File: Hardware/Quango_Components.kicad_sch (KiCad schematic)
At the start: 112 parts, among them J1 Conn_01x12_Male, J2 Conn_01x12_Male, J3 Conn_01x12_Male, J4 Conn_01x12_Male, J5 SWD_Header, J6 Eurorack_10_pin_power, Q1 MMBT3904, U1 LM1117-3.3, U2 STM32G473V, U3 LM1117-5.0, U4 PS508, U5 MCP6002, U6 AS3364, U7 AS3364, U8 AD5676, U9 MCP48CMB21, Y1 8MHz 20pF

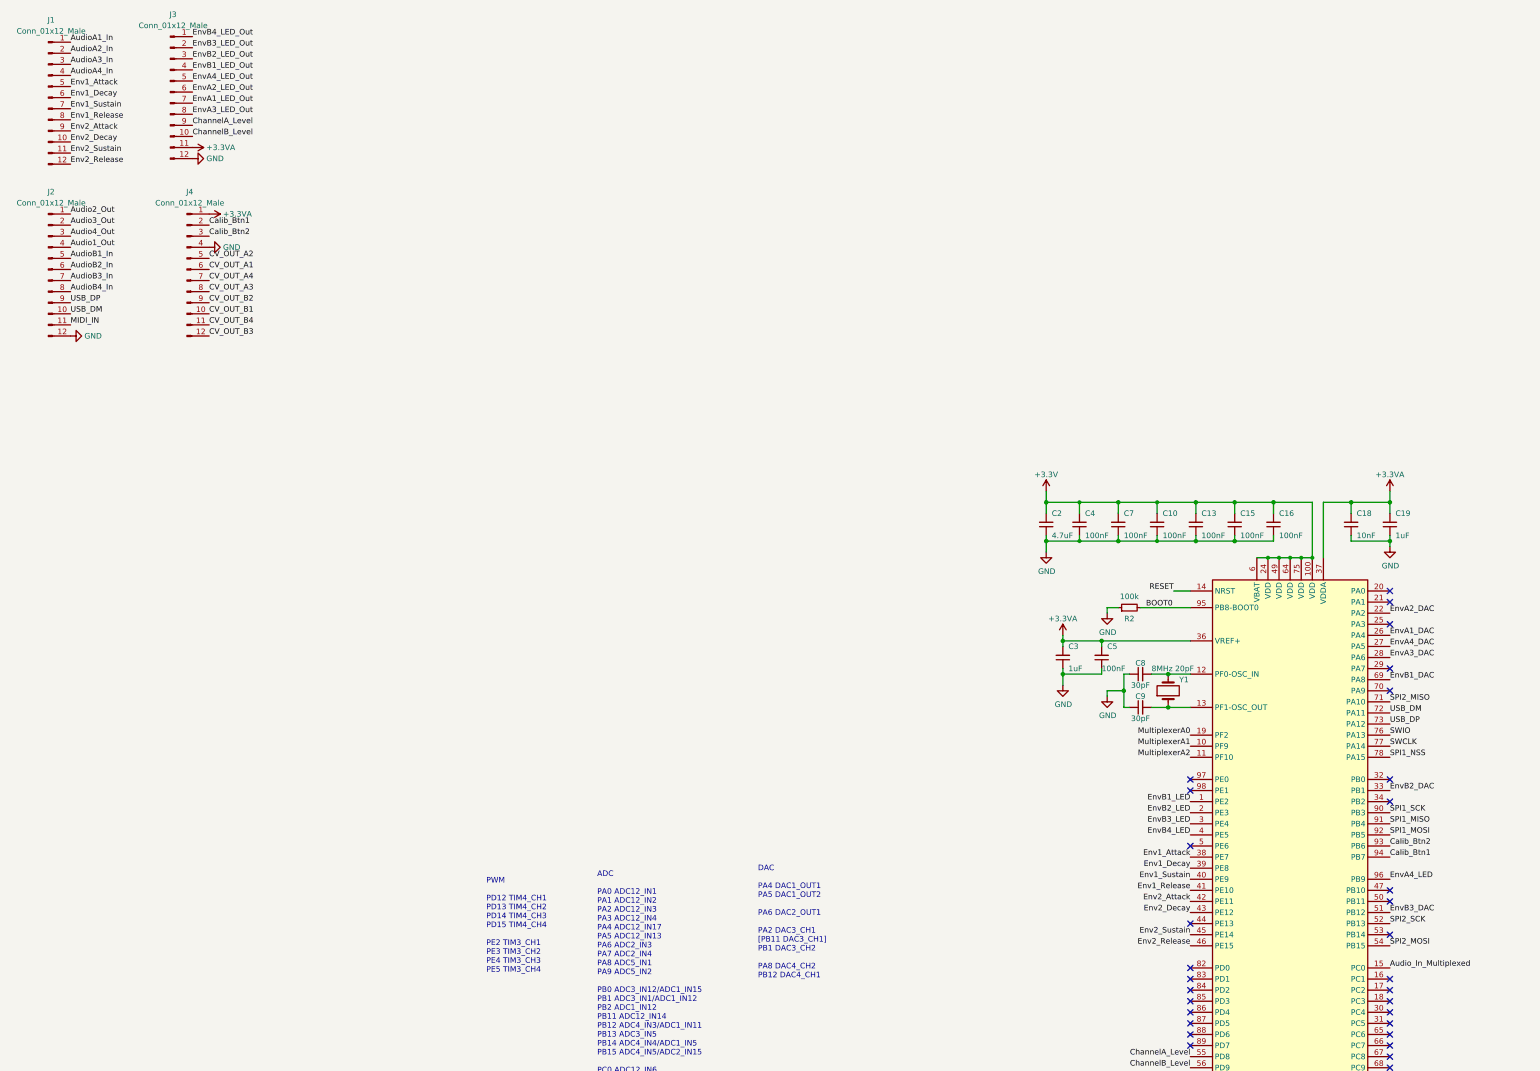
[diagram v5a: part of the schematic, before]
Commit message: First draft of signal routing done
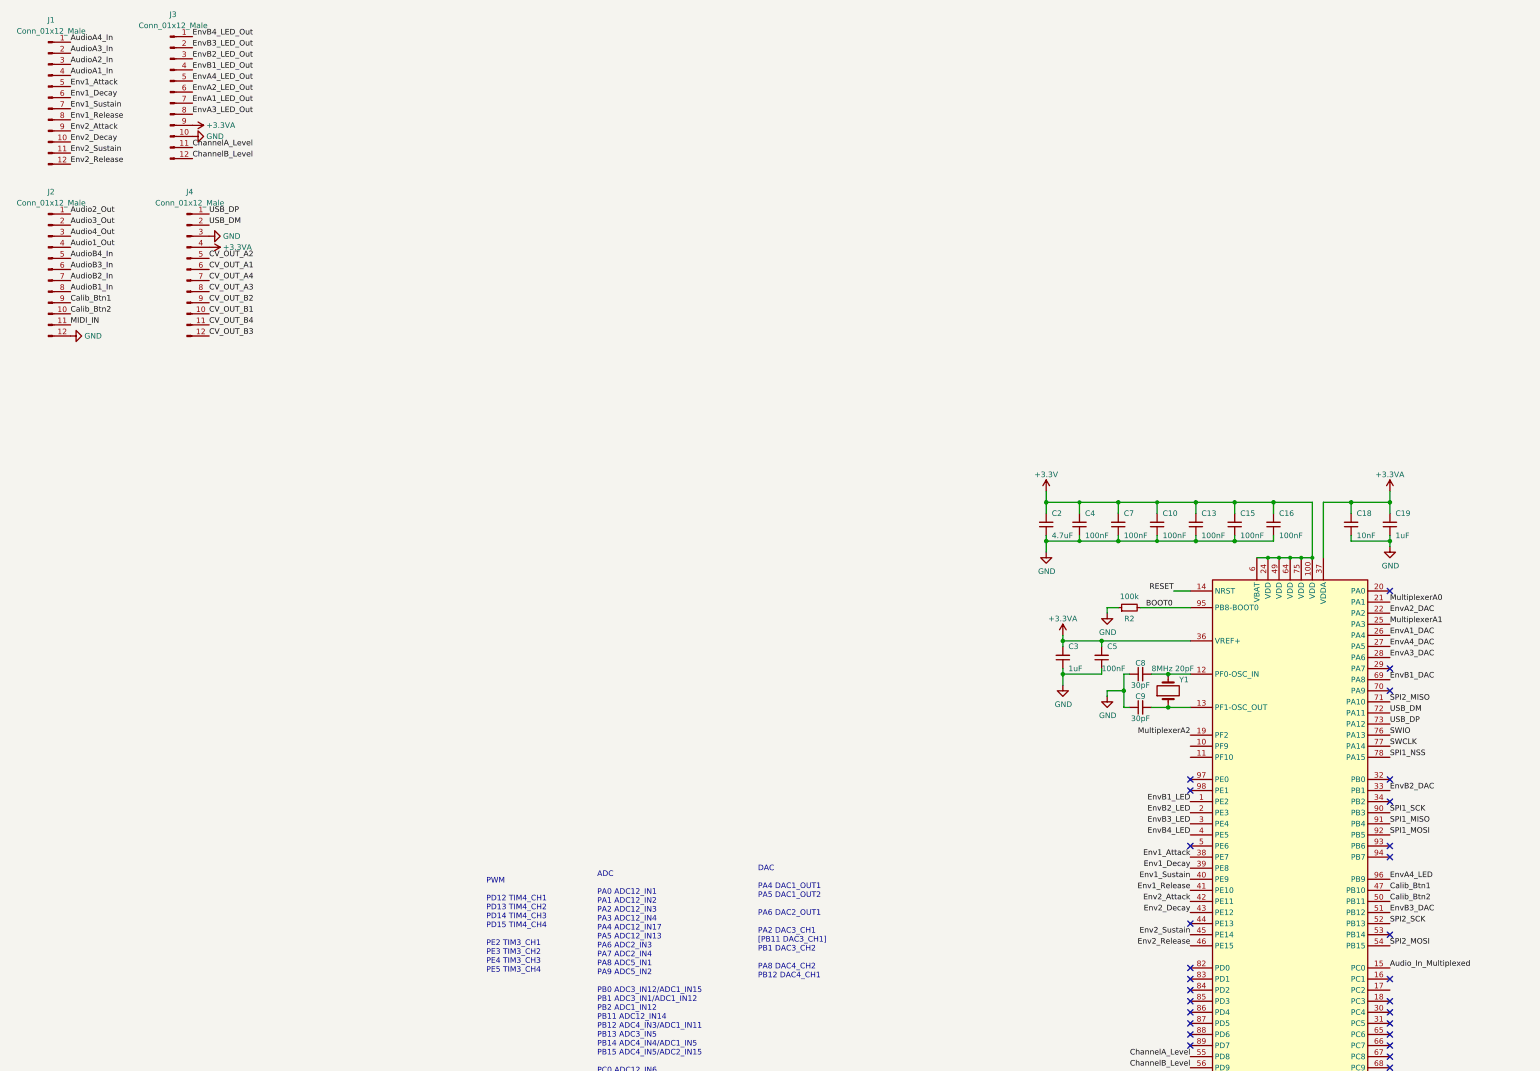
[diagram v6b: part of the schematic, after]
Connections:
- net +3.3VA: now also J3.9 (Pin_9), J4.4 (Pin_4); no longer J3.11 (Pin_11), J4.1 (Pin_1)
- net AudioA1_In: now also J1.4 (Pin_4); no longer J1.1 (Pin_1)
- net AudioA2_In: now also J1.3 (Pin_3); no longer J1.2 (Pin_2)
- net AudioA3_In: now also J1.2 (Pin_2); no longer J1.3 (Pin_3)
- net AudioA4_In: now also J1.1 (Pin_1); no longer J1.4 (Pin_4)
- net AudioB1_In: now also J2.8 (Pin_8); no longer J2.5 (Pin_5)
- net AudioB2_In: now also J2.7 (Pin_7); no longer J2.6 (Pin_6)
- net AudioB3_In: now also J2.6 (Pin_6); no longer J2.7 (Pin_7)
- net AudioB4_In: now also J2.5 (Pin_5); no longer J2.8 (Pin_8)
- net Calib_Btn1: now also J2.9 (Pin_9), U2.47 (PB10); no longer J4.2 (Pin_2), U2.94 (PB7)
- net Calib_Btn2: now also J2.10 (Pin_10), U2.50 (PB11); no longer J4.3 (Pin_3), U2.93 (PB6)
- net ChannelA_Level: now also J3.11 (Pin_11); no longer J3.9 (Pin_9)
- net ChannelB_Level: now also J3.12 (Pin_12); no longer J3.10 (Pin_10)
- net GND: now also J3.10 (Pin_10), J4.3 (Pin_3); no longer J3.12 (Pin_12), J4.4 (Pin_4)
- net MultiplexerA0: now also U2.21 (PA1); no longer U2.19 (PF2)
- net MultiplexerA1: now also U2.25 (PA3); no longer U2.10 (PF9)
- net MultiplexerA2: now also U2.19 (PF2); no longer U2.11 (PF10)
- net USB_DM: now also J4.2 (Pin_2); no longer J2.10 (Pin_10)
- net USB_DP: now also J4.1 (Pin_1); no longer J2.9 (Pin_9)
- no-connect marks 38 -> 35
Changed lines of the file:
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@@
   (no_connect (at 53.34 134.62))
   (no_connect (at 53.34 144.78))
-  (no_connect (at 99.06 111.76))
   (no_connect (at 99.06 66.04))
   (no_connect (at 53.34 154.94))
   (no_connect (at 99.06 142.24))
-  (no_connect (at 99.06 45.72))
   (no_connect (at 53.34 137.16))
   (no_connect (at 99.06 154.94))
   (no_connect (at 53.34 86.36))
+  (no_connect (at 99.06 101.6))
   (no_connect (at 53.34 147.32))
   (no_connect (at 99.06 121.92))
@@
   (no_connect (at 99.06 91.44))
   (no_connect (at 99.06 162.56))
-  (no_connect (at 99.06 134.62))
-  (no_connect (at 99.06 114.3))
+  (no_connect (at 99.06 104.14))
   (no_connect (at 53.34 119.38))
   (no_connect (at 99.06 152.4))
   (no_connect (at 53.34 139.7))
-  (no_connect (at 99.06 50.8))
   (no_connect (at 99.06 86.36))
   (no_connect (at 99.06 137.16))
@@
     (effects (font (size 1.27 1.27)) (justify right bottom))
   )
-  (label "AudioA4_In" (at -203.2 -74.93 0)
+  (label "AudioA4_In" (at -203.2 -82.55 0)
     (effects (font (size 1.27 1.27)) (justify left bottom))
   )
@@
     (effects (font (size 1.27 1.27)) (justify right bottom))
   )
-  (label "ChannelB_Level" (at -175.26 -60.96 0)
+  (label "ChannelB_Level" (at -175.26 -55.88 0)
     (effects (font (size 1.27 1.27)) (justify left bottom))
   )
@@
     (effects (font (size 1.27 1.27)) (justify left bottom))
   )
-  (label "USB_DP" (at -203.2 -22.86 0)
+  (label "USB_DP" (at -171.45 -43.18 0)
     (effects (font (size 1.27 1.27)) (justify left bottom))
   )
@@
     (effects (font (size 1.27 1.27)) (justify right bottom))
   )
-  (label "Calib_Btn2" (at 99.06 101.6 0)
+  (label "Calib_Btn2" (at 99.06 114.3 0)
     (effects (font (size 1.27 1.27)) (justify left bottom))
   )
@@
     (effects (font (size 1.27 1.27)) (justify right bottom))
   )
-  (label "MultiplexerA0" (at 53.34 76.2 180)
-    (effects (font (size 1.27 1.27)) (justify right bottom))
+  (label "MultiplexerA0" (at 99.06 45.72 0)
+    (effects (font (size 1.27 1.27)) (justify left bottom))
   )
   (label "MultiplexerA1" (at 123.19 227.33 180)
@@
     (effects (font (size 1.27 1.27)) (justify left bottom))
   )
-  (label "MultiplexerA1" (at 53.34 78.74 180)
-    (effects (font (size 1.27 1.27)) (justify right bottom))
+  (label "MultiplexerA1" (at 99.06 50.8 0)
+    (effects (font (size 1.27 1.27)) (justify left bottom))
   )
   (label "MultiplexerA0" (at 123.19 224.79 180)
@@
     (effects (font (size 1.27 1.27)) (justify right bottom))
   )
-  (label "AudioA2_In" (at -203.2 -80.01 0)
+  (label "AudioA2_In" (at -203.2 -77.47 0)
     (effects (font (size 1.27 1.27)) (justify left bottom))
   )
@@
     (effects (font (size 1.27 1.27)) (justify right bottom))
   )
-  (label "USB_DM" (at -203.2 -20.32 0)
+  (label "USB_DM" (at -171.45 -40.64 0)
     (effects (font (size 1.27 1.27)) (justify left bottom))
   )
@@
     (effects (font (size 1.27 1.27)) (justify left bottom))
   )
-  (label "AudioA1_In" (at -203.2 -82.55 0)
+  (label "AudioA1_In" (at -203.2 -74.93 0)
     (effects (font (size 1.27 1.27)) (justify left bottom))
   )
@@
     (effects (font (size 1.27 1.27)) (justify right bottom))
   )
-  (label "Calib_Btn1" (at 99.06 104.14 0)
+  (label "Calib_Btn1" (at 99.06 111.76 0)
     (effects (font (size 1.27 1.27)) (justify left bottom))
   )
@@
     (effects (font (size 1.27 1.27)) (justify left bottom))
   )
-  (label "AudioB1_In" (at -203.2 -33.02 0)
+  (label "AudioB1_In" (at -203.2 -25.4 0)
     (effects (font (size 1.27 1.27)) (justify left bottom))
   )
@@
     (effects (font (size 1.27 1.27)) (justify right bottom))
   )
-  (label "AudioB2_In" (at -203.2 -30.48 0)
+  (label "AudioB2_In" (at -203.2 -27.94 0)
     (effects (font (size 1.27 1.27)) (justify left bottom))
   )
@@
     (effects (font (size 1.27 1.27)) (justify left bottom))
   )
-  (label "AudioB4_In" (at -203.2 -25.4 0)
+  (label "AudioB4_In" (at -203.2 -33.02 0)
     (effects (font (size 1.27 1.27)) (justify left bottom))
   )
@@
     (effects (font (size 1.27 1.27)) (justify left bottom))
   )
-  (label "ChannelA_Level" (at -175.26 -63.5 0)
+  (label "ChannelA_Level" (at -175.26 -58.42 0)
     (effects (font (size 1.27 1.27)) (justify left bottom))
   )
@@
     (effects (font (size 1.27 1.27)) (justify left bottom))
   )
-  (label "AudioA3_In" (at -203.2 -77.47 0)
+  (label "AudioA3_In" (at -203.2 -80.01 0)
     (effects (font (size 1.27 1.27)) (justify left bottom))
   )
@@
     (effects (font (size 1.27 1.27)) (justify left bottom))
   )
-  (label "Calib_Btn1" (at -171.45 -40.64 0)
+  (label "Calib_Btn1" (at -203.2 -22.86 0)
     (effects (font (size 1.27 1.27)) (justify left bottom))
   )
@@
     (effects (font (size 1.27 1.27)) (justify right bottom))
   )
-  (label "MultiplexerA2" (at 53.34 81.28 180)
+  (label "MultiplexerA2" (at 53.34 76.2 180)
     (effects (font (size 1.27 1.27)) (justify right bottom))
   )
@@
     (effects (font (size 1.27 1.27)) (justify right bottom))
   )
-  (label "AudioB3_In" (at -203.2 -27.94 0)
+  (label "AudioB3_In" (at -203.2 -30.48 0)
     (effects (font (size 1.27 1.27)) (justify left bottom))
   )
@@
     (effects (font (size 1.27 1.27)) (justify right bottom))
   )
-  (label "Calib_Btn2" (at -171.45 -38.1 0)
+  (label "Calib_Btn2" (at -203.2 -20.32 0)
     (effects (font (size 1.27 1.27)) (justify left bottom))
   )
@@
     (pin "2")
   )
-  (symbol (lib_id "power:+3.3VA") (at -171.45 -43.18 270) (unit 1)
-    (in_bom yes) (on_board yes) (fields_autoplaced)
-    (property "Reference" "#PWR04" (id 0) (at -175.26 -43.18 0)
+  (symbol (lib_id "power:+3.3VA") (at -171.45 -35.56 270) (unit 1)
+    (in_bom yes) (on_board yes)
+    (property "Reference" "#PWR04" (id 0) (at -175.26 -35.56 0)
       (effects (font (size 1.27 1.27)) hide)
     )
-    (property "Value" "+3.3VA" (id 1) (at -168.275 -43.1801 90)
+    (property "Value" "+3.3VA" (id 1) (at -168.275 -35.5601 90)
       (effects (font (size 1.27 1.27)) (justify left))
     )
-    (property "Footprint" "" (id 2) (at -171.45 -43.18 0)
+    (property "Footprint" "" (id 2) (at -171.45 -35.56 0)
       (effects (font (size 1.27 1.27)) hide)
     )
-    (property "Datasheet" "" (id 3) (at -171.45 -43.18 0)
+    (property "Datasheet" "" (id 3) (at -171.45 -35.56 0)
       (effects (font (size 1.27 1.27)) hide)
     )
@@
     (pin "99")
   )
-  (symbol (lib_id "power:+3.3VA") (at -175.26 -58.42 270) (unit 1)
+  (symbol (lib_id "power:+3.3VA") (at -175.26 -63.5 270) (unit 1)
     (in_bom yes) (on_board yes) (fields_autoplaced)
-    (property "Reference" "#PWR02" (id 0) (at -179.07 -58.42 0)
+    (property "Reference" "#PWR02" (id 0) (at -179.07 -63.5 0)
       (effects (font (size 1.27 1.27)) hide)
     )
-    (property "Value" "+3.3VA" (id 1) (at -172.085 -58.4201 90)
+    (property "Value" "+3.3VA" (id 1) (at -172.085 -63.5001 90)
       (effects (font (size 1.27 1.27)) (justify left))
     )
-    (property "Footprint" "" (id 2) (at -175.26 -58.42 0)
+    (property "Footprint" "" (id 2) (at -175.26 -63.5 0)
       (effects (font (size 1.27 1.27)) hide)
     )
-    (property "Datasheet" "" (id 3) (at -175.26 -58.42 0)
+    (property "Datasheet" "" (id 3) (at -175.26 -63.5 0)
       (effects (font (size 1.27 1.27)) hide)
     )
     (pin "1")
   )
-  (symbol (lib_id "power:GND") (at -175.26 -55.88 90) (unit 1)
+  (symbol (lib_id "power:GND") (at -175.26 -60.96 90) (unit 1)
     (in_bom yes) (on_board yes) (fields_autoplaced)
-    (property "Reference" "#PWR03" (id 0) (at -168.91 -55.88 0)
+    (property "Reference" "#PWR03" (id 0) (at -168.91 -60.96 0)
       (effects (font (size 1.27 1.27)) hide)
     )
-    (property "Value" "GND" (id 1) (at -172.085 -55.8801 90)
+    (property "Value" "GND" (id 1) (at -172.085 -60.9601 90)
       (effects (font (size 1.27 1.27)) (justify right))
     )
-    (property "Footprint" "" (id 2) (at -175.26 -55.88 0)
+    (property "Footprint" "" (id 2) (at -175.26 -60.96 0)
       (effects (font (size 1.27 1.27)) hide)
     )
-    (property "Datasheet" "" (id 3) (at -175.26 -55.88 0)
+    (property "Datasheet" "" (id 3) (at -175.26 -60.96 0)
       (effects (font (size 1.27 1.27)) hide)
     )
@@
     (pin "2")
   )
-  (symbol (lib_id "power:GND") (at -171.45 -35.56 90) (unit 1)
+  (symbol (lib_id "power:GND") (at -171.45 -38.1 90) (unit 1)
     (in_bom yes) (on_board yes) (fields_autoplaced)
-    (property "Reference" "#PWR05" (id 0) (at -165.1 -35.56 0)
+    (property "Reference" "#PWR05" (id 0) (at -165.1 -38.1 0)
       (effects (font (size 1.27 1.27)) hide)
     )
-    (property "Value" "GND" (id 1) (at -168.275 -35.5601 90)
+    (property "Value" "GND" (id 1) (at -168.275 -38.1001 90)
       (effects (font (size 1.27 1.27)) (justify right))
     )
-    (property "Footprint" "" (id 2) (at -171.45 -35.56 0)
+    (property "Footprint" "" (id 2) (at -171.45 -38.1 0)
       (effects (font (size 1.27 1.27)) hide)
     )
-    (property "Datasheet" "" (id 3) (at -171.45 -35.56 0)
+    (property "Datasheet" "" (id 3) (at -171.45 -38.1 0)
       (effects (font (size 1.27 1.27)) hide)
     )
